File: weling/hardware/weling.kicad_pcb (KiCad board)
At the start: 2 copper layers, 40 x 30.5 mm, 22 parts, among them J1 USB_C_Receptacle_USB2.0_14P, J2 Connector, SW1 BOOT, U1 CH552G, U2 AMS1117-3.3

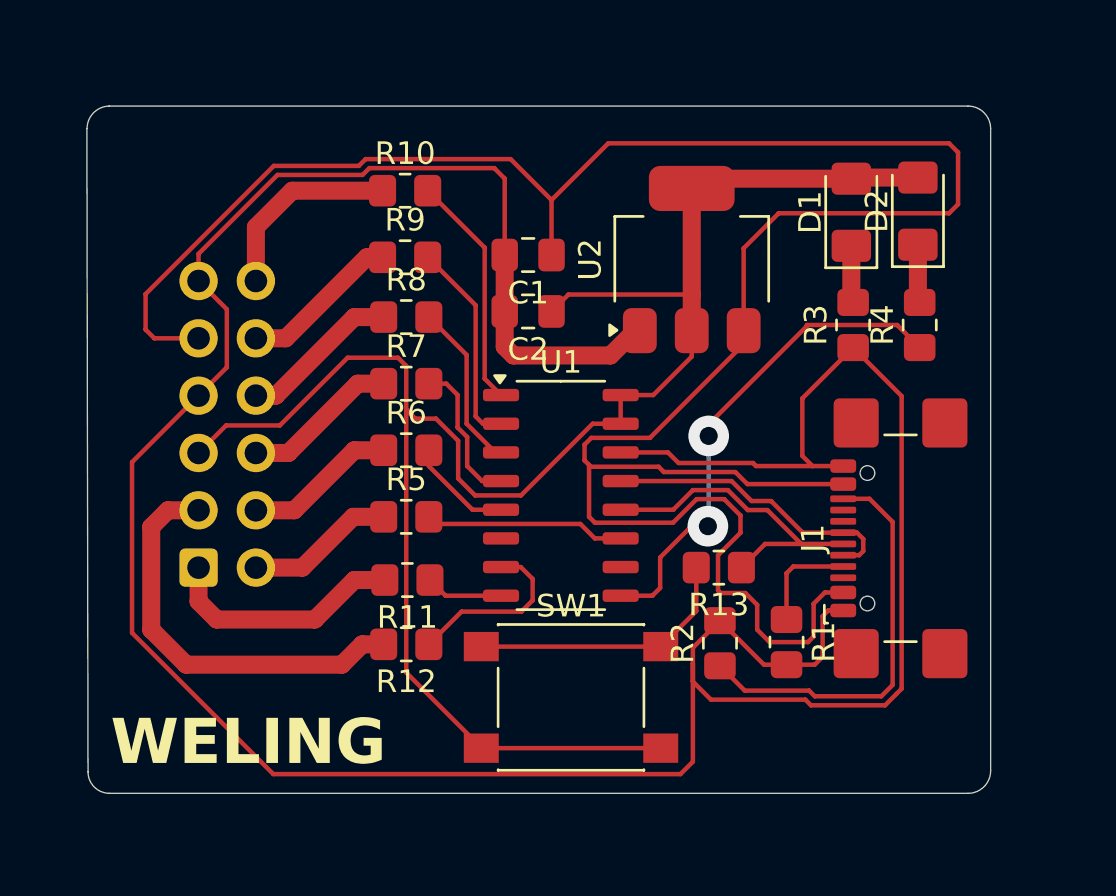
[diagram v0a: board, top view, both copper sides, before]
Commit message: feat: add decoupling capacitor
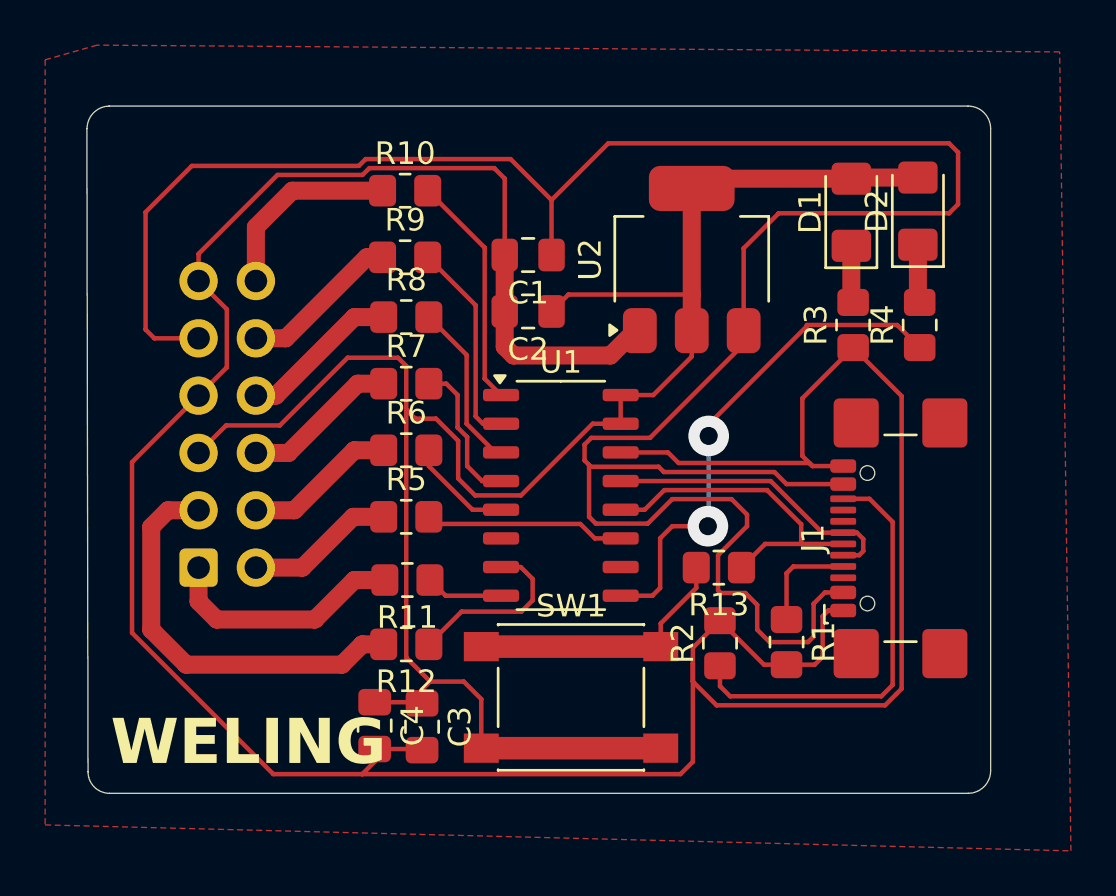
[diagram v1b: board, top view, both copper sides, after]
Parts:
- added C3: 100nF, Capacitor_SMD:C_0805_2012Metric_Pad1.18x1.45mm_HandSolder, F.Cu at (131.3, 91.0)
- added C4: 10uF, Capacitor_SMD:C_0805_2012Metric_Pad1.18x1.45mm_HandSolder, F.Cu at (129.2, 91.0)
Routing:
- net +3.3V: track 80.0 -> 84.2 mm
- net GND: track 134.4 -> 137.9 mm
- net +5V: track 107.8 -> 110.4 mm
- net Net-(J1-CC2): track 18.3 -> 18.8 mm
- net UDP: track 14.3 -> 14.8 mm
- added copper zone on F.Cu, net +3.3V
